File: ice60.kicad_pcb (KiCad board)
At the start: 2 copper layers, 284.7 x 94.2 mm, 195 parts, among them J1 SWD, J2 JST SH 4-pin, SW0 SW_Push, SW1 MX_SW_solder, SW10 MX_SW_solder, SW11 MX_SW_solder, SW12 MX_SW_solder, SW13 MX_SW_solder, SW14 MX_SW_solder, SW15 MX_SW_solder, SW16 MX_SW_solder, SW17 MX_SW_solder, SW18 MX_SW_solder, SW19 MX_SW_solder, SW2 MX_SW_solder, SW20 MX_SW_solder, SW21 MX_SW_solder, SW22 MX_SW_solder, SW23 MX_SW_solder, SW24 MX_SW_solder, SW25 MX_SW_solder, SW26 MX_SW_solder, SW27 MX_SW_solder, SW28 MX_SW_solder, SW29 MX_SW_solder, SW3 MX_SW_solder, SW30 MX_SW_solder, SW31 MX_SW_solder, SW32 MX_SW_solder, SW33 MX_SW_solder, SW34 MX_SW_solder, SW35 MX_SW_solder, SW36 MX_SW_solder, SW37 MX_SW_solder, SW38 MX_SW_solder, SW39 MX_SW_solder, SW4 MX_SW_solder, SW40 MX_SW_solder, SW41 MX_SW_solder, SW42 MX_SW_solder, SW43 MX_SW_solder, SW44 MX_SW_solder, SW45 MX_SW_solder, SW46 MX_SW_solder, SW47 MX_SW_solder, SW48 MX_SW_solder, SW49 MX_SW_solder, SW5 MX_SW_solder, SW50 MX_SW_solder, SW51 MX_SW_solder, SW52 MX_SW_solder, SW53 MX_SW_solder, SW54 MX_SW_solder, SW55 MX_SW_solder, SW56 MX_SW_solder, SW57 MX_SW_solder, SW58 MX_SW_solder, SW59 MX_SW_solder, SW6 MX_SW_solder, SW60 MX_SW_solder, SW61 MX_SW_solder, SW62 MX_SW_solder, SW63 MX_SW_solder, SW64 MX_SW_solder, SW65 MX_SW_solder, SW66 MX_SW_solder, SW67 MX_SW_solder, SW68 MX_SW_solder, SW69 MX_SW_solder, SW7 MX_SW_solder, SW70 MX_SW_solder, SW71 MX_SW_solder, SW72 MX_SW_solder, SW73 MX_SW_solder, SW74 MX_SW_solder, SW75 MX_SW_solder, SW76 MX_SW_solder, SW77 MX_SW_solder, SW78 MX_SW_solder, SW79 MX_SW_solder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

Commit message: add capslock in-switch LED indicator
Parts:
- added D67: LED, marbastlib-mx:LED_MX_3mm, F.Cu at (44.9, 82.5)
- added D68: LED, marbastlib-mx:LED_MX_3mm-FLIPPED, F.Cu at (49.7, 82.5)
- added R6: 470, Resistor_SMD:R_0402_1005Metric, B.Cu at (40.6, 82.6)
- moved D29 6.97 mm to (54.1, 79.9)
- moved D15 6.41 mm to (51.7, 48.9), turned to 180 degrees
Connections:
- SW16 pad 1: Net-(D15-Pad2) -> COL00
- SW16 pad 2: COL00 -> Net-(D15-Pad2)
- SW31 pad 1: Net-(D29-Pad2) -> COL00
- SW31 pad 2: COL00 -> Net-(D29-Pad2)
- SW73 pad : Net-(D61-Pad2) -> (no net)
- SW74 pad : Net-(D61-Pad2) -> (no net)
- U1 pad 35: unconnected-(U1-Pad35) -> CAPSLCK
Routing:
- net CAPSLCK: track 0.00 -> 39.4 mm
- net COL00: track 129.8 -> 146.1 mm
- net ROW1: track 272.4 -> 260.0 mm
- net Net-(R6-Pad2): track 0.00 -> 11.7 mm
- net ROW0: track 291.7 -> 302.1 mm
- net COL01: track 163.2 -> 173.6 mm
- net ROW2: track 305.6 -> 298.1 mm
- net Net-(D29-Pad2): track 14.8 -> 17.0 mm
- net ROW3: track 309.5 -> 311.0 mm
- net ROW4: track 317.1 -> 317.7 mm
- net Net-(D15-Pad2): track 3.87 -> 4.52 mm

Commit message: tweak JST placement
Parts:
- moved D16 3.57 mm to (81.8, 51.3)
- moved J2 0.79 mm to (66.8, 47.3)
- moved R4 0.48 mm to (89.4, 67.9)
- moved D41 0.11 mm to (278.3, 70.3)
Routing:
- net Net-(D16-Pad2): track 4.78 -> 8.35 mm
- net D_P: track 11.4 -> 12.3 mm
- net D_N: track 11.8 -> 12.6 mm
- net GND: vias 11 -> 12

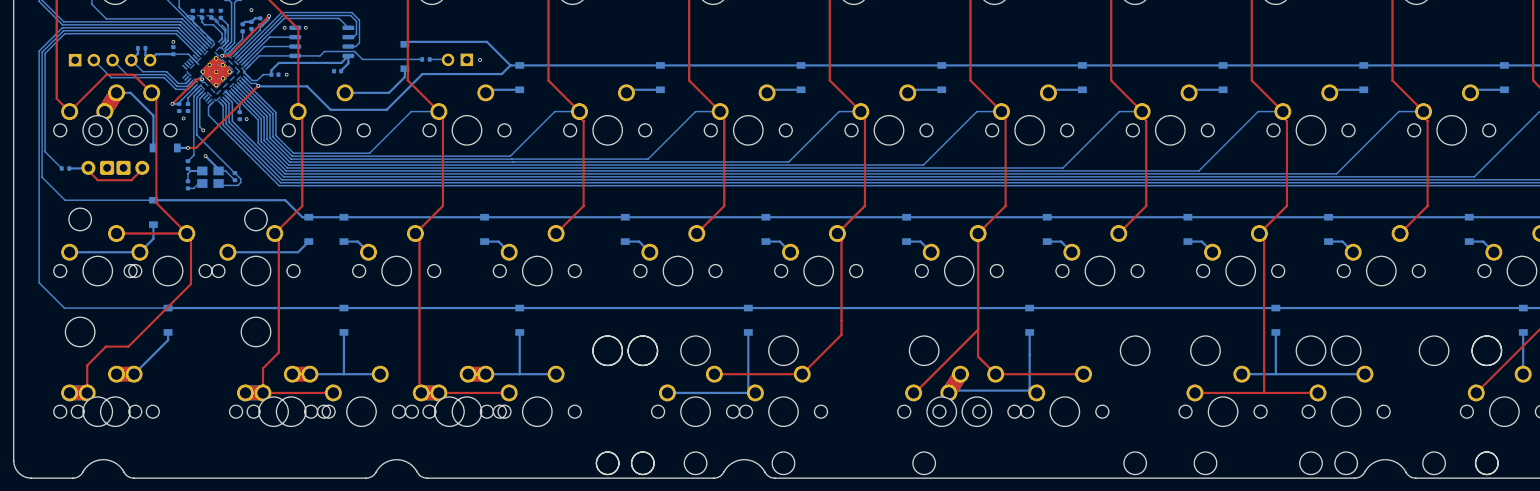
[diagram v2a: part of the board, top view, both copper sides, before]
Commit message: add some layout indicators to silkscreen
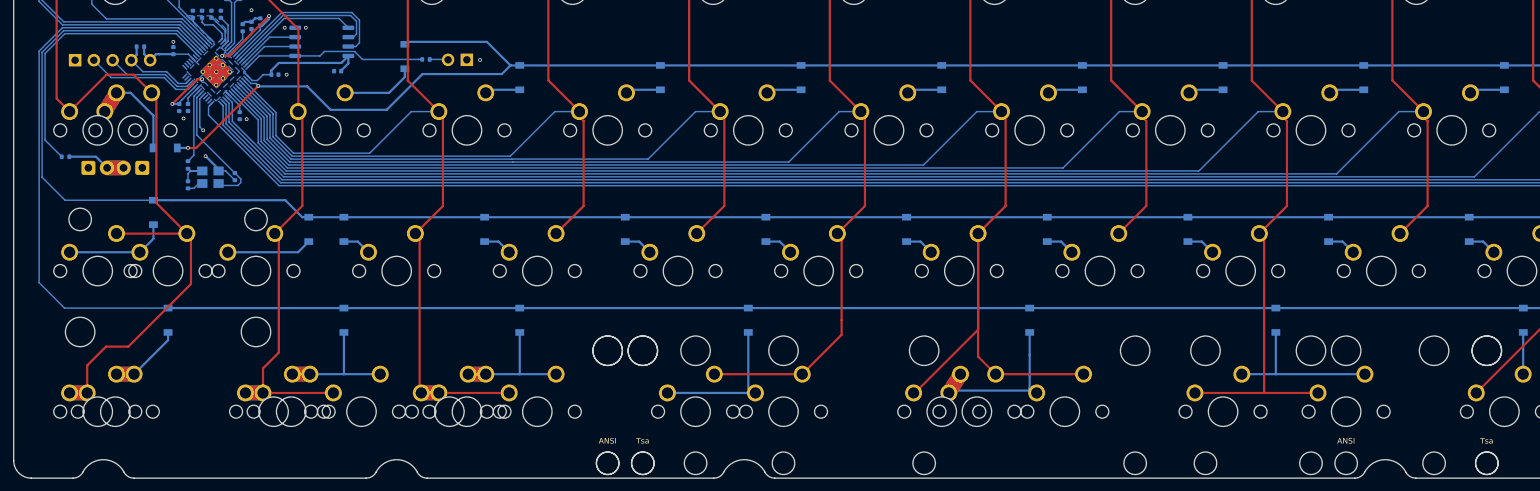
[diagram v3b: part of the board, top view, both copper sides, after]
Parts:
- moved D67 4.76 mm to (49.7, 82.5)
- moved D68 4.76 mm to (44.9, 82.5)
- moved R6 1.59 mm to (40.6, 81.0)
- moved R1 0.28 mm to (50.7, 66.1)
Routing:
- net CAPSLCK: track 39.4 -> 37.8 mm
- net Net-(D67-Pad2): track 11.7 -> 10.2 mm
- net GND: track 38.1 -> 38.8 mm
